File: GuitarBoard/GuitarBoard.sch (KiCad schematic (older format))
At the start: 18 parts

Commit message: Finalized schematic. Need to finish add on boards before making pcb
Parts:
- removed J?: TopRight, symbol Connector:Conn_01x06_Female
- removed J?: TopLeft, symbol Connector:Conn_01x06_Female
- removed J?: BotLeft, symbol Connector:Conn_01x06_Female
- removed J?: BotRight, symbol Connector:Conn_01x06_Female
- removed J?: Amp, symbol audioJacks:AudioJack2
- added J4: FXALeft, Connector_PinSocket_2.54mm:PinSocket_1x04_P2.54mm_Vertical, symbol Connector:Conn_01x04_Female
- added J5: FXARight, Connector_PinSocket_2.54mm:PinSocket_1x04_P2.54mm_Vertical, symbol Connector:Conn_01x04_Female
- added J6: FXBLeft, Connector_PinSocket_2.54mm:PinSocket_1x04_P2.54mm_Vertical, symbol Connector:Conn_01x04_Female
- added J7: FXBRight, Connector_PinSocket_2.54mm:PinSocket_1x04_P2.54mm_Vertical, symbol Connector:Conn_01x04_Female
- added J9: Amp, Connector_PinSocket_2.54mm:PinSocket_1x04_P2.54mm_Vertical, symbol Connector:Conn_01x04_Female
- BT1: renamed from BT?; footprint (none) -> Connector_PinSocket_2.54mm:PinSocket_1x02_P2.54mm_Vertical
- C1: renamed from C?; footprint (none) -> libraries:C_Flat_L7.2_H6.5
- J1, J8: renamed from J?; footprint (none) -> Connector_PinSocket_2.54mm:PinSocket_1x02_P2.54mm_Vertical
- J2: renamed from J?; footprint (none) -> Connector_PinSocket_2.54mm:PinSocket_1x03_P2.54mm_Vertical
- J3: renamed from J?; footprint (none) -> Connector_PinSocket_2.54mm:PinSocket_1x01_P2.54mm_Vertical
- RV1, RV2: renamed from RV?; footprint (none) -> Connector_PinSocket_2.54mm:PinSocket_1x03_P2.54mm_Vertical
- SW1: renamed from SW?; footprint (none) -> Connector_PinSocket_2.54mm:PinSocket_1x02_P2.54mm_Vertical
- SW2, SW3, SW4, SW5: renamed from SW?; footprint (none) -> Connector_PinSocket_2.54mm:PinSocket_1x03_P2.54mm_Vertical
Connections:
- net labels added: Amp
- wire segments 81 -> 70

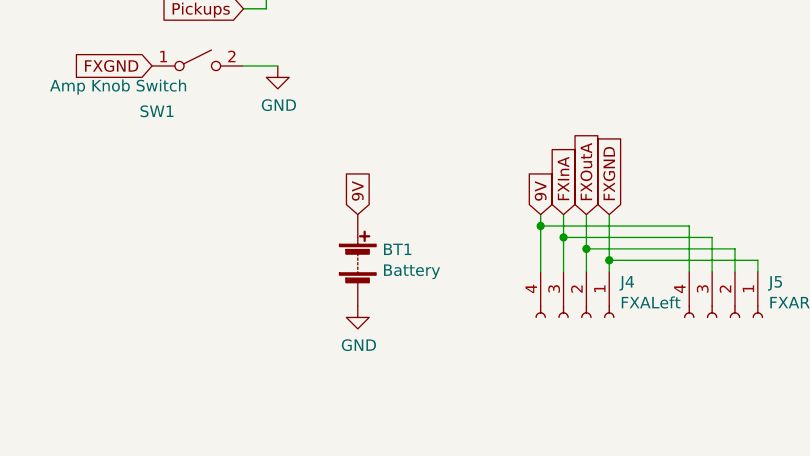
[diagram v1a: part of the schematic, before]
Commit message: Added early version of add on board and reverse polarity protection to mainboard
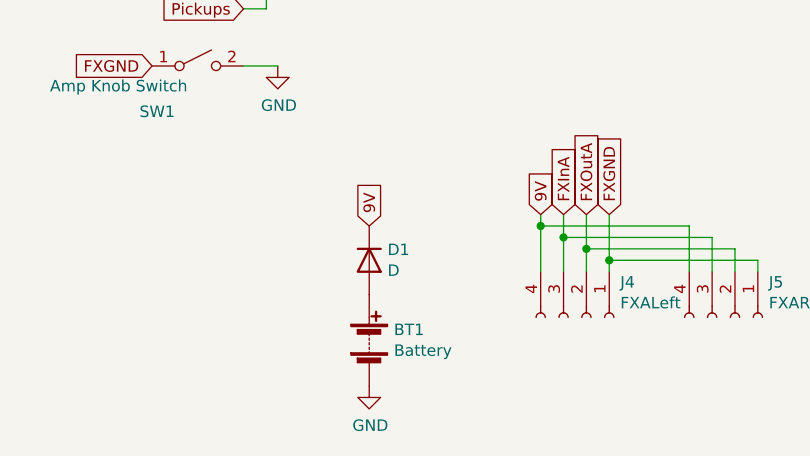
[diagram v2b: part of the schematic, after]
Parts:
- added D1: D, Diode_THT:D_DO-41_SOD81_P10.16mm_Horizontal, symbol Device:D
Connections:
- net 9V: now also D1.1 (K); no longer BT1.1 (+)
- new net: BT1.1 (+), D1.2 (A)
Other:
- moved on the sheet: BT1
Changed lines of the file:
@@
 L Device:Battery BT1
 U 1 1 60619513
-P 4300 4900
-F 0 "BT1" H 4408 4946 50  0000 L CNN
-F 1 "Battery" H 4408 4855 50  0000 L CNN
-F 2 "Connector_PinSocket_2.54mm:PinSocket_1x02_P2.54mm_Vertical" V 4300 4960 50  0001 C CNN
-F 3 "~" V 4300 4960 50  0001 C CNN
-	1    4300 4900
+P 4350 5250
+F 0 "BT1" H 4458 5296 50  0000 L CNN
+F 1 "Battery" H 4458 5205 50  0000 L CNN
+F 2 "Connector_PinSocket_2.54mm:PinSocket_1x02_P2.54mm_Vertical" V 4350 5310 50  0001 C CNN
+F 3 "~" V 4350 5310 50  0001 C CNN
+	1    4350 5250
 	1    0    0    -1
 $EndComp
@@
 L power:GND #PWR04
 U 1 1 6061A385
-P 4300 5100
-F 0 "#PWR04" H 4300 4850 50  0001 C CNN
-F 1 "GND" H 4305 4927 50  0000 C CNN
-F 2 "" H 4300 5100 50  0001 C CNN
-F 3 "" H 4300 5100 50  0001 C CNN
-	1    4300 5100
+P 4350 5450
+F 0 "#PWR04" H 4350 5200 50  0001 C CNN
+F 1 "GND" H 4355 5277 50  0000 C CNN
+F 2 "" H 4350 5450 50  0001 C CNN
+F 3 "" H 4350 5450 50  0001 C CNN
+	1    4350 5450
 	1    0    0    -1
 $EndComp
@@
 Wire Wire Line
 	3900 3500 4000 3500
-Text GLabel 4300 4700 1    50   Input ~ 0
+Text GLabel 4350 4750 1    50   Input ~ 0
 9V
 Text GLabel 3400 4050 0    50   Input ~ 0
@@
 Wire Wire Line
 	8000 4700 8000 4950
+$Comp
+L Device:D D1
+U 1 1 6063E1F4
+P 4350 4900
+F 0 "D1" V 4304 4980 50  0000 L CNN
+F 1 "D" V 4395 4980 50  0000 L CNN
+F 2 "Diode_THT:D_DO-41_SOD81_P10.16mm_Horizontal" H 4350 4900 50  0001 C CNN
+F 3 "~" H 4350 4900 50  0001 C CNN
+	1    4350 4900
+	0    1    1    0
+$EndComp
 $EndSCHEMATC

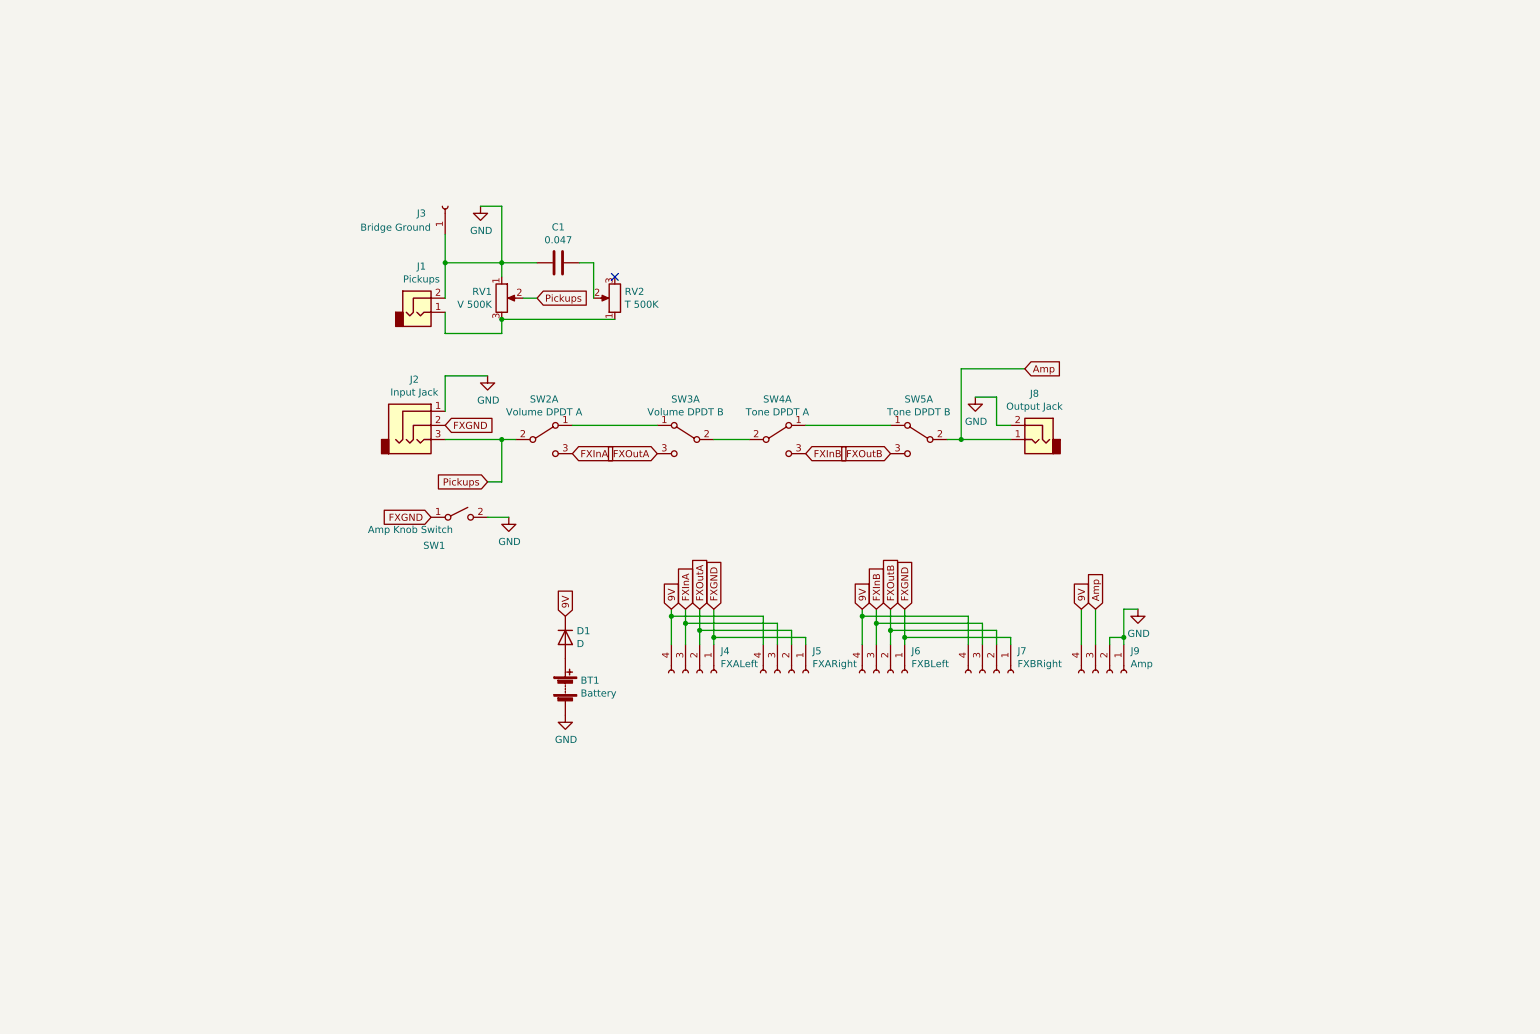
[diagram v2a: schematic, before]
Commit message: Merging pedals into one board
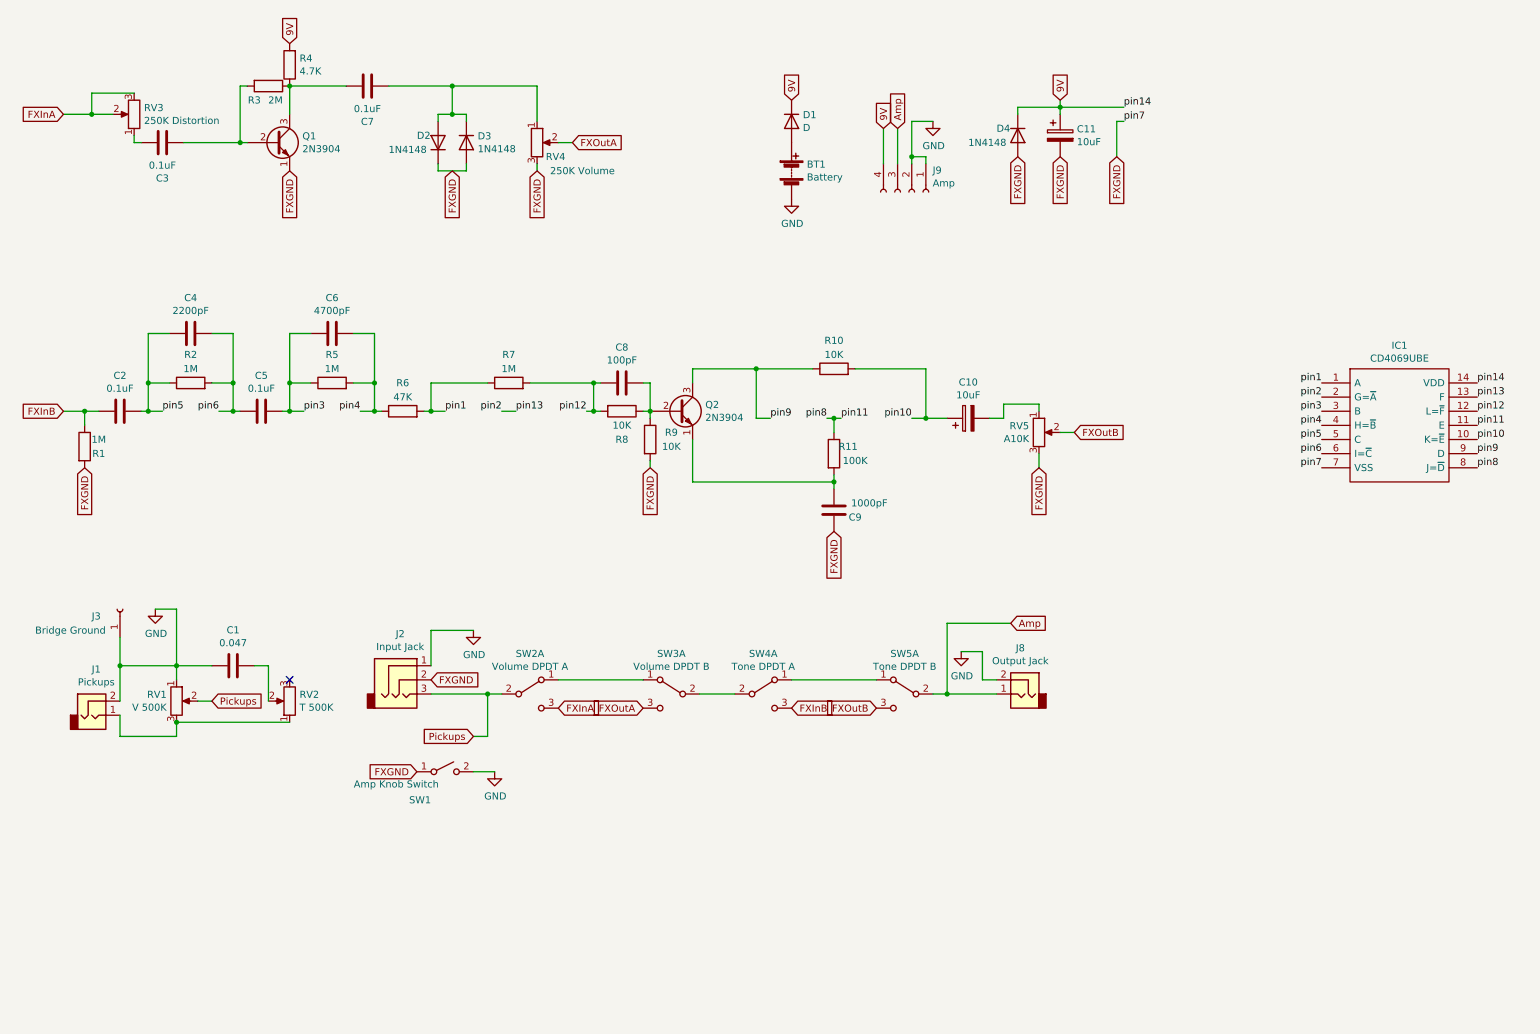
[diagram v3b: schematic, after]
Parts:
- removed J4: FXALeft, Connector_PinSocket_2.54mm:PinSocket_1x04_P2.54mm_Vertical, symbol Connector:Conn_01x04_Female
- removed J5: FXARight, Connector_PinSocket_2.54mm:PinSocket_1x04_P2.54mm_Vertical, symbol Connector:Conn_01x04_Female
- removed J6: FXBLeft, Connector_PinSocket_2.54mm:PinSocket_1x04_P2.54mm_Vertical, symbol Connector:Conn_01x04_Female
- removed J7: FXBRight, Connector_PinSocket_2.54mm:PinSocket_1x04_P2.54mm_Vertical, symbol Connector:Conn_01x04_Female
- added C10, C11: 10uF, Capacitor_THT:CP_Axial_L10.0mm_D6.0mm_P15.00mm_Horizontal, symbol Device:CP
- added C2, C3, C5, C7: 0.1uF, libraries:C_Flat_L7.2_H6.5, symbol Device:C
- added C4: 2200pF, libraries:C_Flat_L7.2_H6.5, symbol Device:C
- added C6: 4700pF, libraries:C_Flat_L7.2_H6.5, symbol Device:C
- added C8: 100pF, libraries:C_Flat_L7.2_H6.5, symbol Device:C
- added C9: 1000pF, libraries:C_Flat_L7.2_H6.5, symbol Device:C
- added D2, D3, D4: 1N4148, Diode_THT:D_DO-35_SOD27_P7.62mm_Horizontal, symbol Diode:1N4148
- added IC1: CD4069UBE, SamacSys_Parts:DIP794W53P254L1930H508Q14N, symbol SamacSys_Parts:CD4069UBE
- added Q1, Q2: 2N3904, Package_TO_SOT_THT:TO-92_Inline, symbol Transistor_BJT:2N3904
- added R1, R2, R5, R7: 1M, Resistor_THT:R_Axial_DIN0207_L6.3mm_D2.5mm_P10.16mm_Horizontal, symbol Device:R
- added R10, R8, R9: 10K, Resistor_THT:R_Axial_DIN0207_L6.3mm_D2.5mm_P10.16mm_Horizontal, symbol Device:R
- added R11: 100K, Resistor_THT:R_Axial_DIN0207_L6.3mm_D2.5mm_P10.16mm_Horizontal, symbol Device:R
- added R3: 2M, Resistor_THT:R_Axial_DIN0207_L6.3mm_D2.5mm_P10.16mm_Horizontal, symbol Device:R
- added R4: 4.7K, Resistor_THT:R_Axial_DIN0207_L6.3mm_D2.5mm_P10.16mm_Horizontal, symbol Device:R
- added R6: 47K, Resistor_THT:R_Axial_DIN0207_L6.3mm_D2.5mm_P10.16mm_Horizontal, symbol Device:R
- added RV3: 250K Distortion, Potentiometer_THT:Potentiometer_Bourns_3386F_Vertical, symbol Device:R_POT
- added RV4: 250K Volume, Potentiometer_THT:Potentiometer_Bourns_3386F_Vertical, symbol Device:R_POT
- added RV5: A10K, Potentiometer_THT:Potentiometer_Bourns_3386F_Vertical, symbol Device:R_POT
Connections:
- net 9V: now also C11.1, D4.1 (K), IC1.14 (VDD), R4.2
- net FXGND: now also C11.2, C9.1, D2.1 (K), D3.2 (A), D4.2 (A), IC1.7 (VSS), Q1.1 (E), R1.2, R9.2, RV4.3, RV5.3
- net FXInA: now also RV3.2, RV3.3
- net FXInB: now also C2.2, R1.1
- net FXOutA: now also RV4.2
- net FXOutB: now also RV5.2
- new net: C3.1, RV3.1
- new net: C3.2, Q1.2 (B), R3.2
- new net: C7.1, Q1.3 (C), R3.1, R4.1
- new net: C7.2, D2.2 (A), D3.1 (K), RV4.1
- new net: C8.1, Q2.2 (B), R8.1, R9.1
- new net: C9.2, Q2.1 (E), R11.2
- new net: C10.2, RV5.1
- new net pin1: IC1.1 (A), R6.2, R7.1
- new net pin10: C10.1, IC1.10 (K=~E), R10.2
- new net pin11: IC1.11 (E), IC1.8 (J=~D), R11.1
- new net pin12: C8.2, IC1.12 (L=~F), R7.2, R8.2
- new net pin13: IC1.13 (F), IC1.2 (G=~A)
- new net pin3: C5.1, C6.2, IC1.3 (B), R5.1
- new net pin4: C6.1, IC1.4 (H=~B), R5.2, R6.1
- new net pin5: C2.1, C4.2, IC1.5 (C), R2.1
- new net pin6: C4.1, C5.2, IC1.6 (I=~C), R2.2
- new net pin9: IC1.9 (D), Q2.3 (C), R10.1
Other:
- moved on the sheet: BT1, C1, D1, J1, J2, J3, J8, J9, RV1, RV2, SW1, SW2A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

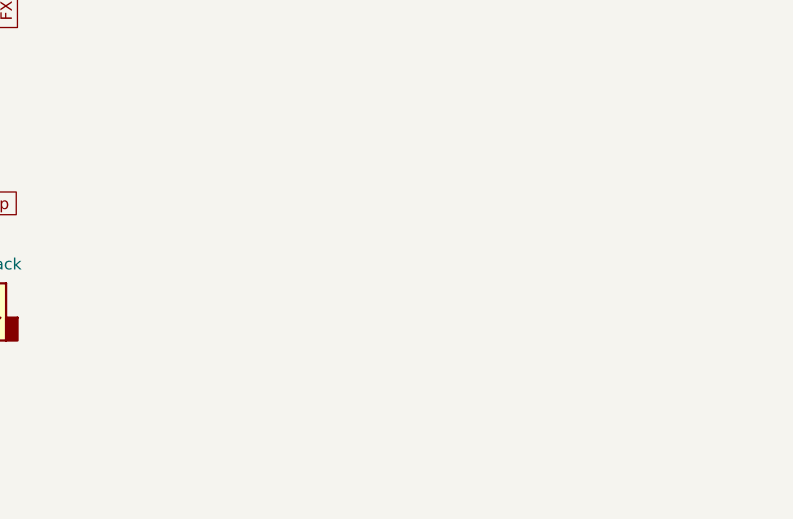
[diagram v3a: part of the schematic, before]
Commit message: Started tracing everything out
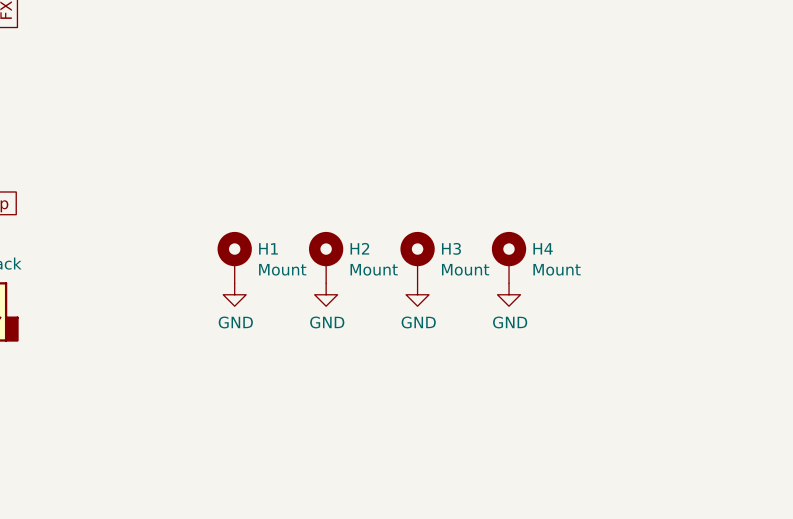
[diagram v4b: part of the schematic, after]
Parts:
- added H1, H2, H3, H4: Mount, MountingHole:MountingHole_2.7mm_Pad, symbol Mechanical:MountingHole_Pad
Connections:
- net GND: now also H1.1, H2.1, H3.1, H4.1
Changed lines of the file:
@@
 	6800 1250 6800 1500
 Connection ~ 6800 1500
+$Comp
+L Mechanical:MountingHole_Pad H1
+U 1 1 608F0DC6
+P 8700 5050
+F 0 "H1" H 8800 5099 50  0000 L CNN
+F 1 "Mount" H 8800 5008 50  0000 L CNN
+F 2 "MountingHole:MountingHole_2.7mm_Pad" H 8700 5050 50  0001 C CNN
+F 3 "~" H 8700 5050 50  0001 C CNN
+	1    8700 5050
+	1    0    0    -1
+$EndComp
+$Comp
+L power:GND #PWR07
+U 1 1 608F1447
+P 8700 5150
+F 0 "#PWR07" H 8700 4900 50  0001 C CNN
+F 1 "GND" H 8705 4977 50  0000 C CNN
+F 2 "" H 8700 5150 50  0001 C CNN
+F 3 "" H 8700 5150 50  0001 C CNN
+	1    8700 5150
+	1    0    0    -1
+$EndComp
+$Comp
+L Mechanical:MountingHole_Pad H2
+U 1 1 608F7664
+P 9100 5050
+F 0 "H2" H 9200 5099 50  0000 L CNN
+F 1 "Mount" H 9200 5008 50  0000 L CNN
+F 2 "MountingHole:MountingHole_2.7mm_Pad" H 9100 5050 50  0001 C CNN
+F 3 "~" H 9100 5050 50  0001 C CNN
+	1    9100 5050
+	1    0    0    -1
+$EndComp
+$Comp
+L Mechanical:MountingHole_Pad H3
+U 1 1 608F7A0A
+P 9500 5050
+F 0 "H3" H 9600 5099 50  0000 L CNN
+F 1 "Mount" H 9600 5008 50  0000 L CNN
+F 2 "MountingHole:MountingHole_2.7mm_Pad" H 9500 5050 50  0001 C CNN
+F 3 "~" H 9500 5050 50  0001 C CNN
+	1    9500 5050
+	1    0    0    -1
+$EndComp
+$Comp
+L Mechanical:MountingHole_Pad H4
+U 1 1 608F7DC8
+P 9900 5050
+F 0 "H4" H 10000 5099 50  0000 L CNN
+F 1 "Mount" H 10000 5008 50  0000 L CNN
+F 2 "MountingHole:MountingHole_2.7mm_Pad" H 9900 5050 50  0001 C CNN
+F 3 "~" H 9900 5050 50  0001 C CNN
+	1    9900 5050
+	1    0    0    -1
+$EndComp
+$Comp
+L power:GND #PWR08
+U 1 1 608F8CBA
+P 9100 5150
+F 0 "#PWR08" H 9100 4900 50  0001 C CNN
+F 1 "GND" H 9105 4977 50  0000 C CNN
+F 2 "" H 9100 5150 50  0001 C CNN
+F 3 "" H 9100 5150 50  0001 C CNN
+	1    9100 5150
+	1    0    0    -1
+$EndComp
+$Comp
+L power:GND #PWR09
+U 1 1 608F9058
+P 9500 5150
+F 0 "#PWR09" H 9500 4900 50  0001 C CNN
+F 1 "GND" H 9505 4977 50  0000 C CNN
+F 2 "" H 9500 5150 50  0001 C CNN
+F 3 "" H 9500 5150 50  0001 C CNN
+	1    9500 5150
+	1    0    0    -1
+$EndComp
+$Comp
+L power:GND #PWR010
+U 1 1 608F9366
+P 9900 5150
+F 0 "#PWR010" H 9900 4900 50  0001 C CNN
+F 1 "GND" H 9905 4977 50  0000 C CNN
+F 2 "" H 9900 5150 50  0001 C CNN
+F 3 "" H 9900 5150 50  0001 C CNN
+	1    9900 5150
+	1    0    0    -1
+$EndComp
 $EndSCHEMATC

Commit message: Made new board. Still need to lay out all the traces
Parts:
- added RV6: 250K Input Volume, Potentiometer_THT:Potentiometer_Bourns_3386F_Vertical, symbol Device:R_POT
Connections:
- net FXGND: now also RV6.1
- net FXInB: now also RV6.2; no longer C2.2, R1.1
- new net: C2.2, R1.1, RV6.3
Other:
- moved on the sheet: C10, C2, C4, C5, C6, C8, C9, Q2, R1, R10, R11, R2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

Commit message: Switched which pedal came first. Added JLC order number location
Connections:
- net FXInA: now also RV6.2; no longer RV3.2, RV3.3
- net FXInB: now also RV3.2, RV3.3; no longer RV6.2
- net FXOutA: now also RV5.2; no longer RV4.2
- net FXOutB: now also RV4.2; no longer RV5.2
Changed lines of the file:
@@
 	-1   0    0    1
 $EndComp
-Text GLabel 800  1200 0    50   Input ~ 0
+Text GLabel 1050 3300 0    50   Input ~ 0
 FXInA
 $Comp
@@
 	4150 1000 3550 1000
 Connection ~ 3550 1000
-Text GLabel 4400 1400 2    50   Input ~ 0
+Text GLabel 8800 3450 2    50   Input ~ 0
 FXOutA
 Wire Wire Line
@@
 Wire Wire Line
 	4150 1600 4150 1550
-Text GLabel 1050 3300 0    50   Input ~ 0
+Text GLabel 800  1200 0    50   Input ~ 0
 FXInB
 $Comp
@@
 Wire Wire Line
 	8300 3350 8200 3350
-Text GLabel 8800 3450 2    50   Input ~ 0
+Text GLabel 4400 1400 2    50   Input ~ 0
 FXOutB
 Wire Wire Line
